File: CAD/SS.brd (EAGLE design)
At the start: 77 x 109 mm, 88 parts, among them Q1 SN74AHC-NOR, Q2 UMD5N, Q4 SN74AHC-AND, Q5 BFP460, Q6 L78L05, Q7 NCP553, T1 MMBTRA104SS

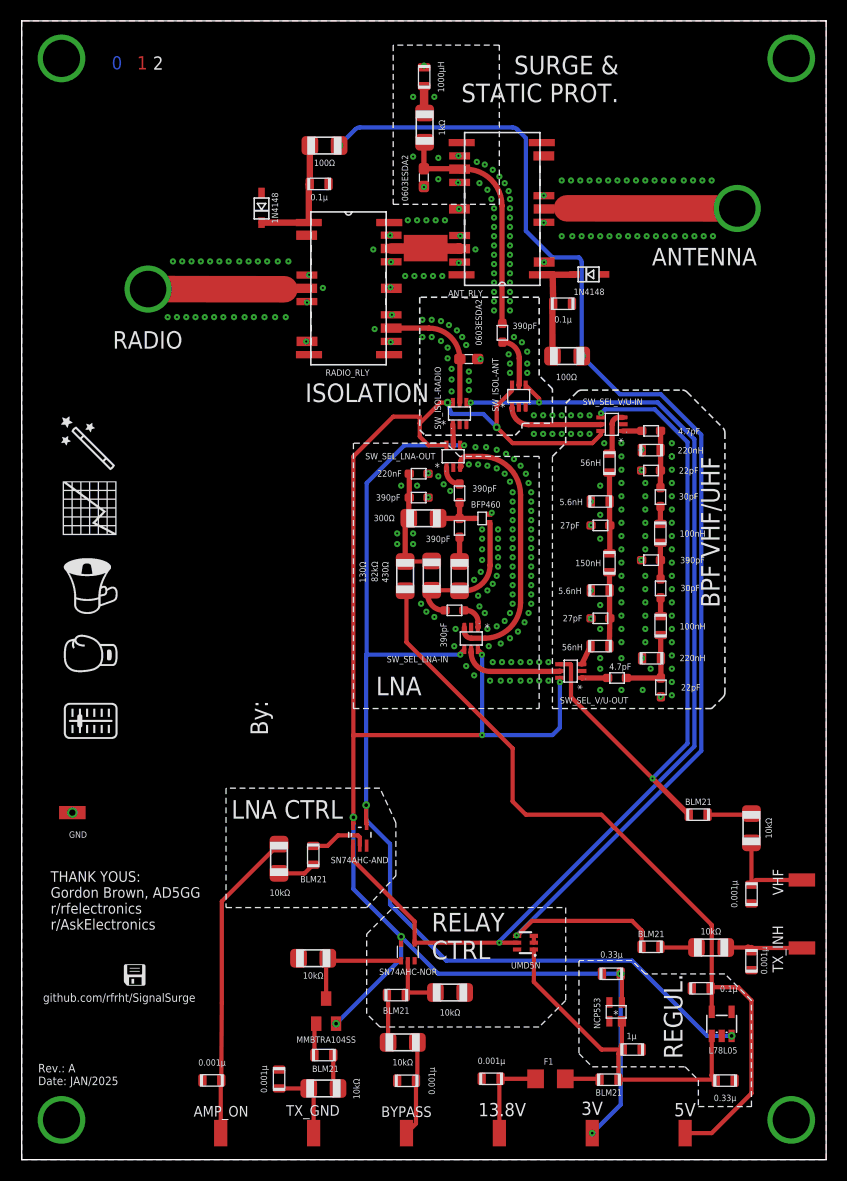
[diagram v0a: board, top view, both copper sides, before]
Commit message: More improvements, check the commit comment
- Fixed BFR460 footprint (it was VERY wrong)
- Zeroed the DRC warnings
- Added rastnest stop on some large RF-involved components
- Named few signal lines
- Improved identification of Pin 1 of RF switches
- Added Test Points
- Better component identification
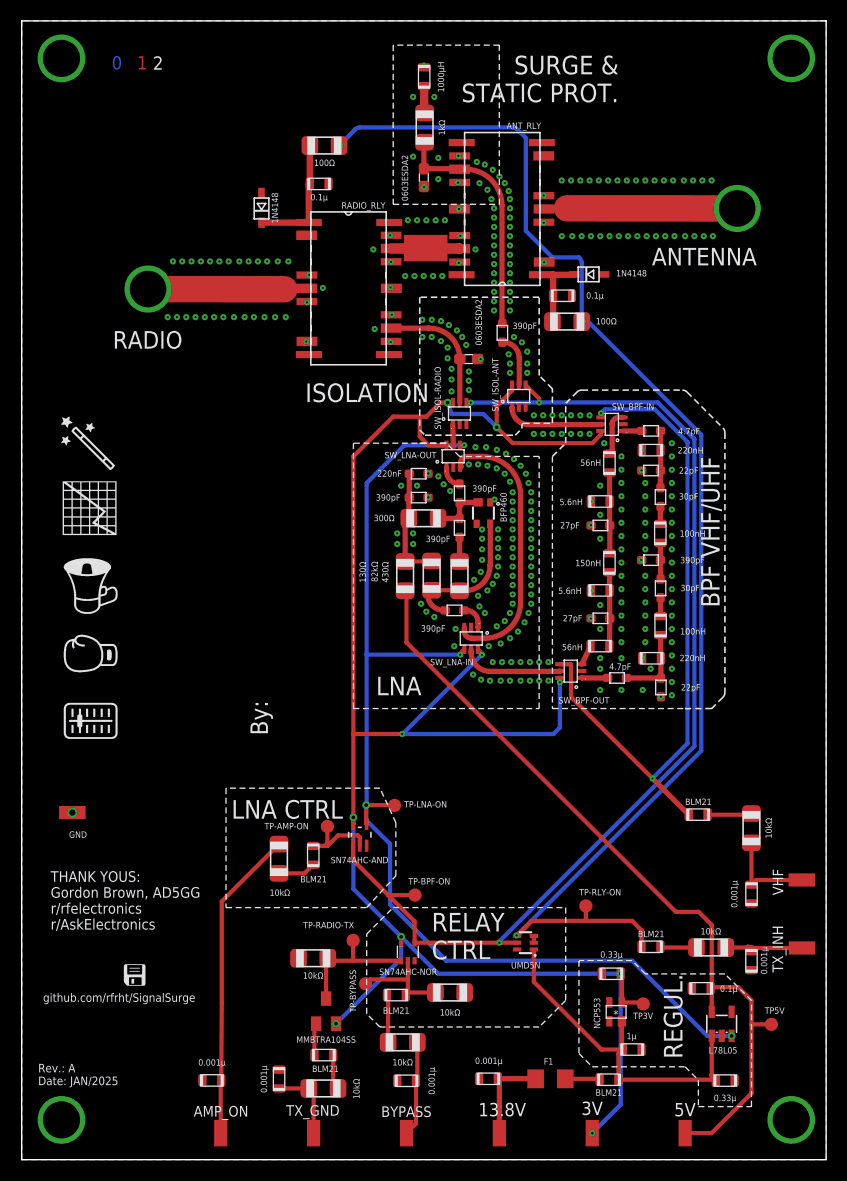
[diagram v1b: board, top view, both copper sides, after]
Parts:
- added TP-AMP-ON, TP-BPF-ON, TP-BYPASS, TP-LNA-ON, TP-RADIO-TX, TP-RLY-ON, TP3V, TP5V: TPB1,27, testpad:B1,27
- Q5: device aarf:TSFP-3 -> aarf:SOT343R
- moved R9 3.30 mm to (52.2, 80.2)
- moved C17 0.76 mm to (51.8, 82.7)
- moved Q5 0.52 mm to (44.2, 61.9)
- moved C13 0.25 mm to (44.7, 7.75)
- renumbered SW_SEL_LNA-IN to SW_LNA-IN, SW_SEL_LNA-OUT to SW_LNA-OUT, SW_SEL_V/U-IN to SW_BPF-IN, SW_SEL_V/U-OUT to SW_BPF-OUT
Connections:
- removed net N$17: C8.P$2, Q5.1, R1.1, R2.2
- removed net N$25: C12.P$1, C9.P$2, Q5.3, R3.1
- new net LNA-IN: C8.P$2, Q5.4, R1.1, R2.2
- new net LNA-OUT: C12.P$1, C9.P$2, Q5.2, R3.1
- net 3V: now also TP3V.TP
- net 5V: now also TP5V.TP
- net AMP_ON: now also TP-AMP-ON.TP
- net BPF_ON: now also TP-BPF-ON.TP
- net FORCE_BYPASS: now also TP-BYPASS.TP
- net GND: now also Q5.1, Q5.3; no longer Q5.2
- net LNA_ON: now also TP-LNA-ON.TP
- net RADIO_TX: now also TP-RADIO-TX.TP
- net RELAY-RX_ON: now also TP-RLY-ON.TP
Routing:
- net N$17: track 13.6 -> 0.00 mm
- net LNA-IN: track 0.00 -> 13.5 mm
- net 3V: track 172.5 -> 178.4 mm
- net LNA-OUT: track 0.00 -> 5.37 mm
- net N$25: track 5.09 -> 0.00 mm
- net FEED-RA: track 12.0 -> 7.66 mm
- net FORCE_BYPASS: track 6.30 -> 10.5 mm
- net LNA_ON: track 101.9 -> 104.6 mm
- net BPF_ON: track 103.2 -> 105.7 mm
- net AMP_ON: track 5.76 -> 7.72 mm
- net RADIO_TX: track 11.0 -> 13.0 mm
- net 5V: track 78.1 -> 77.1 mm
- net RELAY-RX_ON: track 127.8 -> 127.3 mm

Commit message: New: BOM. And minor improvements (more in comments)
- Added a BOM
- Changed L7 footprint to match the Tayo proprietary (1207 footprint)
- Another round of DRC check
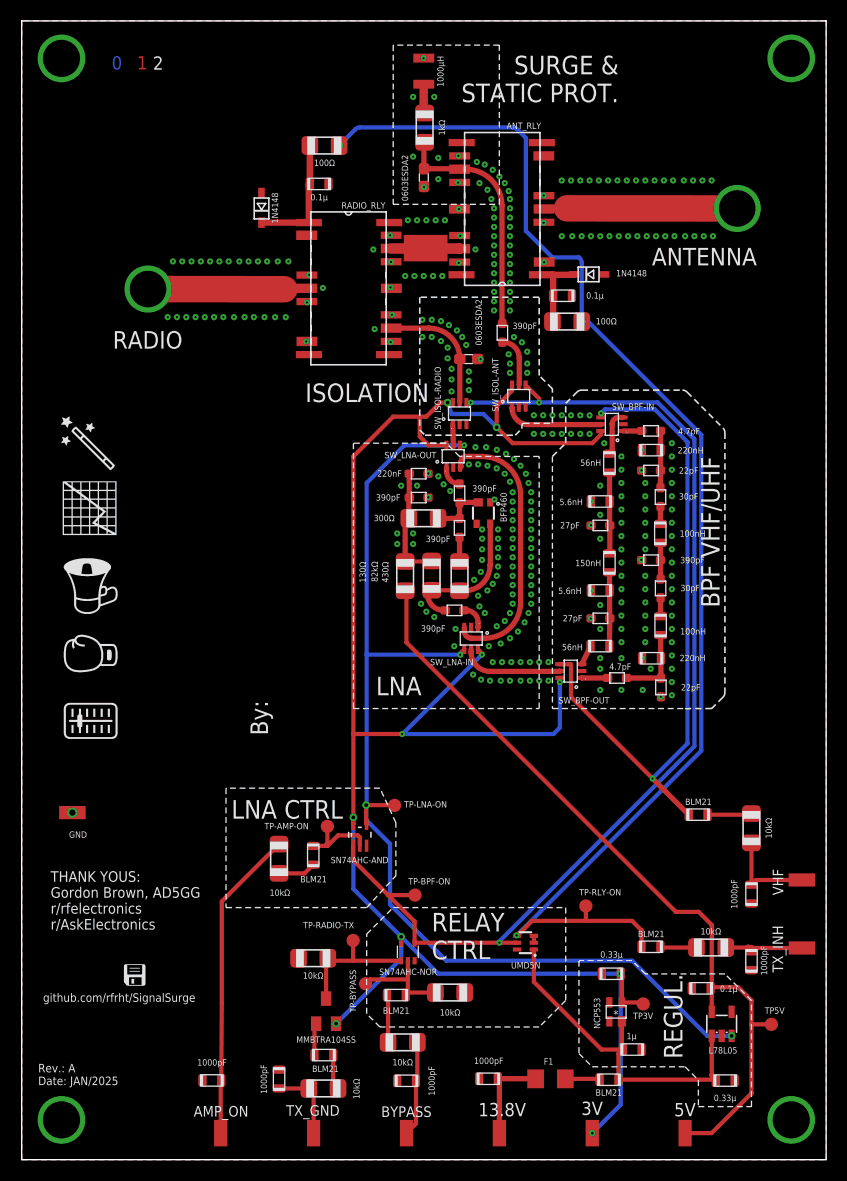
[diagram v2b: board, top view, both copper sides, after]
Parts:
- C13, C14, C15, C16, C19, C20: value 0.001µ -> 1000pF
- L7: device aarf:0805 -> aarf:1207
- moved L7 0.54 mm to (38.5, 104.2)
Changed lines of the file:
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@@
 <drawing>
 <settings>
-<setting alwaysvectorfont="yes"/>
+<setting alwaysvectorfont="no"/>
 <setting verticaltext="up"/>
 </settings>
@@
 <attribute name="VALUE" x="44.3" y="64.246" size="0.6096" layer="21" font="vector" ratio="15" rot="R180" align="center"/>
 </element>
-<element name="C13" library="aarf" package="0805" value="0.001µ" x="44.676" y="7.75" smashed="yes">
+<element name="C13" library="aarf" package="0805" value="1000pF" x="44.676" y="7.75" smashed="yes">
 <attribute name="VALUE" x="44.708" y="9.464" size="0.6096" layer="21" font="vector" ratio="15" align="center"/>
 </element>
-<element name="C14" library="aarf" package="0805" value="0.001µ" x="69.847" y="19.041" smashed="yes" rot="R90">
+<element name="C14" library="aarf" package="0805" value="1000pF" x="69.847" y="19.041" smashed="yes" rot="R90">
 <attribute name="VALUE" x="71.054" y="19.057" size="0.6096" layer="21" font="vector" ratio="15" rot="R90" align="center"/>
 </element>
-<element name="C15" library="aarf" package="0805" value="0.001µ" x="24.642" y="7.72" smashed="yes" rot="R270">
+<element name="C15" library="aarf" package="0805" value="1000pF" x="24.642" y="7.72" smashed="yes" rot="R270">
 <attribute name="VALUE" x="23.181" y="7.704" size="0.6096" layer="21" font="vector" ratio="15" rot="R270" align="center"/>
 </element>
-<element name="C16" library="aarf" package="0805" value="0.001µ" x="36.84" y="7.558" smashed="yes">
+<element name="C16" library="aarf" package="0805" value="1000pF" x="36.84" y="7.558" smashed="yes">
 <attribute name="VALUE" x="39.242" y="7.535" size="0.6096" layer="21" font="vector" ratio="15" rot="R90" align="center"/>
 </element>
@@
 <attribute name="VALUE" x="28.471" y="92.132" size="0.6096" layer="21" font="vector" ratio="15" align="center"/>
 </element>
-<element name="C19" library="aarf" package="0805" value="0.001µ" x="69.85" y="25.423" smashed="yes" rot="R90">
+<element name="C19" library="aarf" package="0805" value="1000pF" x="69.85" y="25.423" smashed="yes" rot="R90">
 <attribute name="VALUE" x="68.199" y="25.423" size="0.6096" layer="21" font="vector" ratio="15" rot="R90" align="center"/>
 </element>
@@
 <attribute name="VALUE" x="63.8427625" y="65.9638" size="0.6096" layer="21" font="vector" ratio="15" rot="R180" align="center"/>
 </element>
-<element name="C20" library="aarf" package="0805" value="0.001µ" x="18.203" y="7.592" smashed="yes">
+<element name="C20" library="aarf" package="0805" value="1000pF" x="18.203" y="7.592" smashed="yes">
 <attribute name="VALUE" x="18.219" y="9.306" size="0.6096" layer="21" font="vector" ratio="15" align="center"/>
 </element>
@@
 <attribute name="VALUE" x="40.22" y="98.783" size="0.6096" layer="21" font="vector" ratio="15" rot="R270" align="center"/>
 </element>
-<element name="L7" library="aarf" package="0805" value="1000µH" x="38.519" y="103.655" smashed="yes" rot="R90">
-<attribute name="VALUE" x="40.132" y="103.636" size="0.6096" layer="21" font="vector" ratio="15" rot="R90" align="center"/>
+<element name="L7" library="aarf" package="1207" value="1000µH" x="38.4682" y="104.1884" smashed="yes" rot="R90">
+<attribute name="VALUE" x="40.0812" y="104.1694" size="0.6096" layer="21" font="vector" ratio="15" rot="R90" align="center"/>
 </element>
 <element name="R13" library="aarf" package="1206" value="10kΩ" x="27.9" y="19.28" smashed="yes" rot="R180">
@@
 <via x="45.24248125" y="63.190121875" extent="1-16" drill="0.2"/>
 <via x="43.92168125" y="76.62671875" extent="1-16" drill="0.2"/>
-<via x="38.506403125" y="104.71911875" extent="1-16" drill="0.2"/>
+<via x="38.455603125" y="105.43031875" extent="1-16" drill="0.2"/>
 <via x="38.506403125" y="93.096078125" extent="1-16" drill="0.2"/>
 <via x="27.518359375" y="84.6937625" extent="1-16" drill="0.2"/>
@@
 <contactref element="R8" pad="1"/>
 <contactref element="L7" pad="P$1"/>
-<wire x1="38.569" y1="100.183" x2="38.519" y2="100.233" width="0.6096" layer="1"/>
-<wire x1="38.519" y1="100.233" x2="38.519" y2="102.755" width="0.8128" layer="1"/>
+<wire x1="38.569" y1="100.183" x2="38.46466875" y2="100.28733125" width="0.6096" layer="1"/>
+<wire x1="38.46466875" y1="100.28733125" x2="38.4842" y2="102.9374" width="0.8128" layer="1"/>
 </signal>
 <signal name="N$8">

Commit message: Board: Shrinked board a bit to fit JLCPCB $2 tier
Board was a bit larger than 10 cm, shrinked it to fit to the $2 tier

Also; updated README
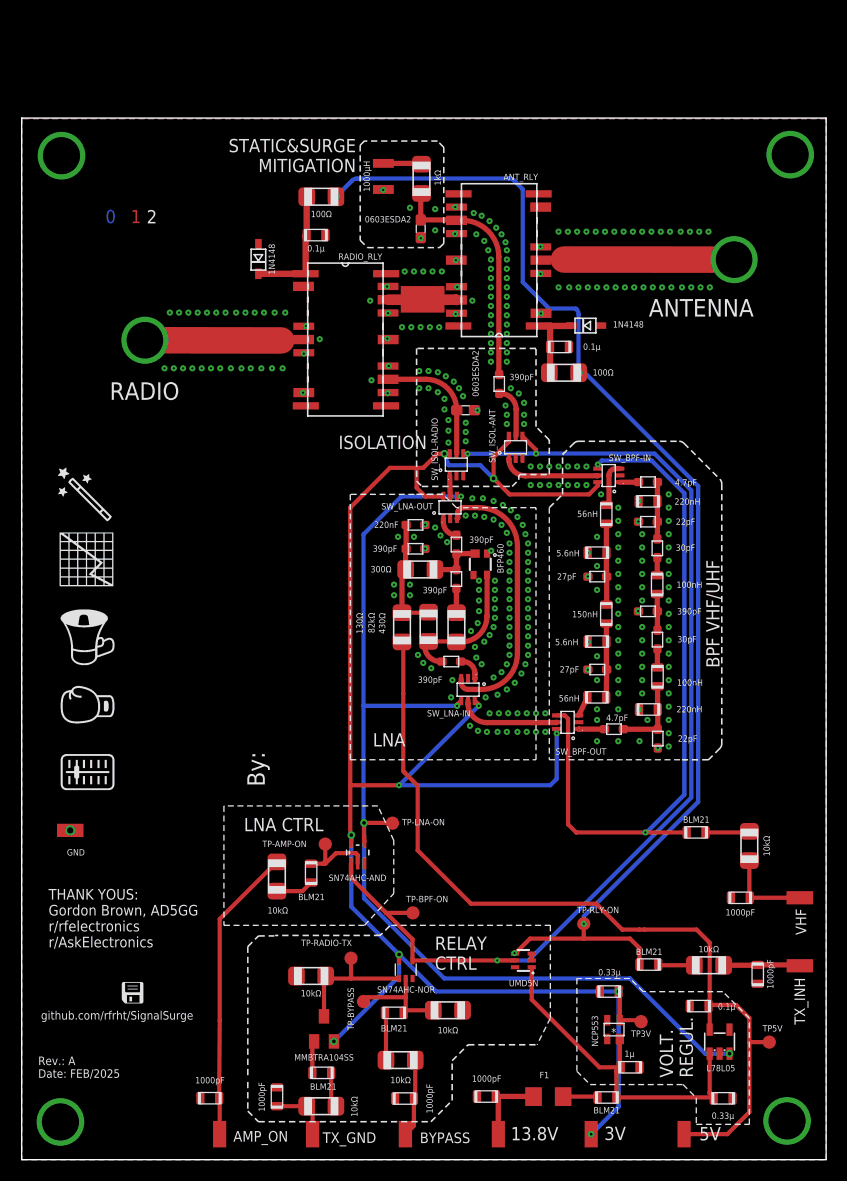
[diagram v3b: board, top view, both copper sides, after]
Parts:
- moved L7 10.8 mm to (34.6, 94.1), turned to 270 degrees
- moved ANTENNA 4.91 mm to (68.2, 86.1)
- moved C1 4.91 mm to (60.0, 64.9)
- moved C11 4.91 mm to (37.7, 60.8)
- moved C17 4.91 mm to (51.5, 77.8)
- moved C25 4.91 mm to (45.7, 74.2)
- moved C3 4.91 mm to (60.8, 58.5)
- moved C4 4.91 mm to (59.9, 52.5)
- moved C6 4.91 mm to (55.1, 55.8)
- moved C7 4.91 mm to (55.1, 46.9)
- moved D1 4.91 mm to (38.2, 89.1)
- moved L2 4.91 mm to (60.8, 55.0)
- moved L8 4.91 mm to (56.0, 52.2)
- moved Q5 4.91 mm to (43.9, 57.0)
- moved R8 4.91 mm to (38.3, 93.9)
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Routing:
- net RELAY-RX_ON: track 127.3 -> 118.5 mm, vias 3 -> 4
- net 5V: track 77.1 -> 83.1 mm
- net 3V: track 178.4 -> 173.6 mm
- net SEL_BPF_VHF: track 63.8 -> 67.2 mm
- net LNA_ON: track 104.6 -> 101.4 mm
- net N$15: track 30.0 -> 28.4 mm
- net N$10: track 9.14 -> 7.50 mm
- net N$16: track 7.31 -> 5.75 mm
- net N$9: track 8.89 -> 7.33 mm
- net BPF_ON: track 105.7 -> 104.2 mm
- net N$2: track 2.80 -> 3.68 mm
- net N$12: track 9.03 -> 8.36 mm
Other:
- board size 77 x 109 mm -> 77 x 99.7 mm
- board text added: "Rev.: A Date: FEB/2025"
- board text added: "STATIC&SURGE MITIGATION"
- board text added: "VOLT. REGUL."
- board text removed: "REGUL."
- board text removed: "Rev.: A Date: JAN/2025"
- board text removed: "SURGE & STATIC PROT."

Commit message: Starring: Rev. B
Resolves: #1 #2 #4 #5 #10 #11 #12 #13 #14 #15 #16 #17

In a nutshell:
- Fixed UMD5N placement issue
- Improved UMD5N footprint
- Improved NCP553 footprint
- Improved SN74-OR footprint
- Changed connectors to SMA
- Fixed the 5V voltage regulator
- Fixed lotsa BOM errors
- Improved and recalculated coplanar waveguide
- Updated VHF BPF component values
- Added a TP for VHF BPF
- Added three u.FL connectors/pads to help debugging
- Pretty much this is it!
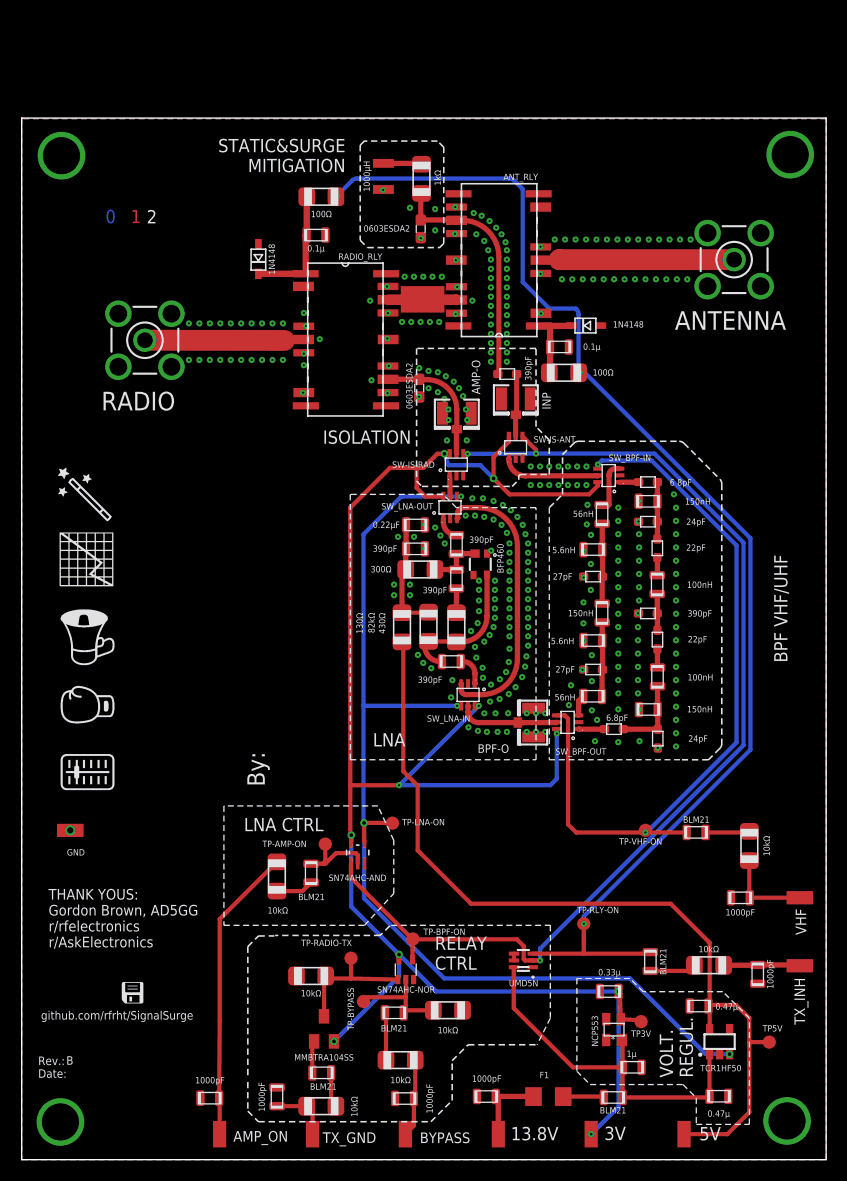
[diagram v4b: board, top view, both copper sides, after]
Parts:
- removed ANTENNA: ANTENNA, wirepad:SMD1,27-2,54
- removed RADIO: RADIO, wirepad:SMD1,27-2,54
- added TP-VHF-ON: TPB1,27, testpad:B1,27
- added X1: ANTENNA, aarf:SMA-RF
- added X2: RADIO, aarf:SMA-RF
- added X3: INP, adafruit:U.FL
- added X4: AMP-O, adafruit:U.FL
- added X5: BPF-O, adafruit:U.FL
- C1, C27: value 4.7pF -> 6.8pF
- C10, C12, C8, C9: device aarf:GRM18 -> aarf:0805
- C11: value 220nF -> 0.22µF; device aarf:GRM18 -> aarf:0805
- C2, C26: value 22pF -> 24pF
- C21: value 0.33µ -> 0.47µ
- C22: value 0.1µ -> 0.47µ
- C3, C5: value 30pF -> 22pF
- L1, L4: value 220nH -> 150nH
- Q6: value L78L05 -> TCR1HF50; device aarf:SOT23-5L -> aarf:SC-74A
- moved D4 4.91 mm to (38.1, 73.8), turned to 90 degrees
- moved TP-BPF-ON 2.50 mm to (37.4, 21.1)
- moved C25 1.22 mm to (46.5, 75.2), turned to 180 degrees
- moved FB1 0.60 mm to (56.6, 5.96)
- moved L10 0.50 mm to (54.7, 58.4)
- moved SW_LNA-IN 0.50 mm to (42.7, 44.5)
- moved C21 0.45 mm to (66.7, 6.07)
- moved L11 0.41 mm to (54.7, 49.7)
- moved L8 0.41 mm to (55.6, 52.3)
- moved L6 0.41 mm to (54.6, 44.3)
- moved C6 0.40 mm to (54.7, 55.8)
- moved C7 0.40 mm to (54.7, 46.9)
- moved L9 0.40 mm to (55.6, 61.8)
- moved FB2 0.33 mm to (60.2, 19.0), turned to 90 degrees
- moved C23 0.20 mm to (58.4, 8.84)
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- renumbered SW_ISOL-ANT to SW-IS-ANT, SW_ISOL-RADIO to SW-IS-RAD
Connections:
- removed net IN_DECPL: C25.P$2, SW-IS-ANT.5
- removed net N$36: Q2.2, Q2.3
- new net N$17: C25.P$1, SW-IS-ANT.5, X3.3
- new net N$7: Q2.4, Q2.5
- net 13.8V: now also Q2.6; no longer Q2.1
- net AMP+BPF_OUT: now also X4.3
- net ANTENNA: now also X1.1; no longer ANTENNA.1
- net BPF_ON: now also Q2.2; no longer Q2.5
- net BPF_OUT: now also X5.3
- net GND: now also Q2.1, X1.2, X1.3, X1.4, X1.5, X2.2, X2.3, X2.4, X2.5, X3.2, X4.2, X5.2; no longer Q2.6
- net RADIO: now also X2.1; no longer RADIO.1
- net RELAY-RX_ON: now also Q2.3; no longer Q2.4
- net SEL_BPF_VHF: now also TP-VHF-ON.TP
- net TO_BPF: now also C25.P$2; no longer C25.P$1
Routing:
- net N$17: track 0.00 -> 6.01 mm
- net IN_DECPL: track 4.84 -> 0.00 mm
- net SEL_BPF_VHF: track 67.2 -> 71.5 mm
- net RELAY-RX_ON: track 118.5 -> 120.9 mm, vias 4 -> 3
- net BPF_ON: track 104.2 -> 106.3 mm
- net N$27: track 3.48 -> 4.44 mm
- net 13.8V: track 34.0 -> 34.7 mm
- net N$7: track 0.00 -> 0.65 mm
- net N$36: track 0.65 -> 0.00 mm
- net LNA-BYPASS: track 25.7 -> 26.4 mm
- net N$13: track 3.36 -> 3.96 mm
- net UHF-IN: track 4.24 -> 4.83 mm
- net 3V: track 173.6 -> 173.0 mm
- net N$3: track 2.33 -> 2.83 mm
- net RADIO: vias 1 -> 0
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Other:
- board text added: ">LAST_DATE_TIME"
- board text added: ">REVISION"
- board text added: "Rev.: Date:"
- board text removed: "Rev.: A Date: FEB/2025"
